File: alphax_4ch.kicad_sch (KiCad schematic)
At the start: 124 parts, among them J3 Conn_01x01, J4 Conn_01x01, J6 430451012, J7 Conn_01x01, J8 Conn_01x01, M1 Module-power_12and5V-0.1, M2 Module-ign8-0.2, M3 Module-vr-discrete-0.4, M6 Module-ign8-0.2, M8 Module-vr-discrete-0.4, M9 Module-knock-0.2, P1 33311-24AW-2, P2 33311-24AW-2, P3 Pad, P4 Pad

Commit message: Fab export
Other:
- note added: "4.5k UP (default)/3.3k DOWN"
- note added: "CAM HALL PU 5VA: remove R21 5VAS/GND configurable: - remove R4"
- note added: "Test note: IN_CRANK+ line HALL: remove R753_2 VR: remove R1126, R22"
- note added: "Test note: remove 1nf for VR"
- note removed: "1.2k UP (default)/4.5k DOWN"
- note removed: "CAM HALL PU 5VA: remove R21 5VAS configurable: - remove R4"
- note removed: "IN_CRANK+ line HALL: remove R753_2"
- note removed: "remove 1nf for VR"
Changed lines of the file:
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@@
   (title_block
     (title "AlphaECU 4chan powered by rusEFI")
-    (date "2023-03-19")
-    (rev "G")
+    (date "2023-05-11")
+    (rev "H")
     (company "rusEFI")
     (comment 7 "http://rusefi.com/s/alphax4ch")
@@
     (effects (font (size 1.27 1.27)) (justify left bottom))
   )
-  (text "1.2k UP (default)/4.5k DOWN" (at 299.72 255.27 0)
+  (text "4.5k UP (default)/3.3k DOWN" (at 299.72 255.27 0)
     (effects (font (size 1.27 1.27)) (justify left bottom))
   )
@@
     (effects (font (size 1.27 1.27)) (justify left bottom))
   )
-  (text "CAM HALL PU\n5VA: remove R21\n5VAS configurable: - remove R4"
+  (text "CAM HALL PU\n5VA: remove R21\n5VAS/GND configurable: - remove R4"
     (at 230.505 269.875 0)
     (effects (font (size 1.27 1.27)) (justify left bottom))
@@
     (effects (font (size 1.27 1.27)) (justify right bottom))
   )
+  (text "4.5k UP (default)/3.3k DOWN" (at 299.72 280.67 0)
+    (effects (font (size 1.27 1.27)) (justify left bottom))
+  )
   (text "GND test pads" (at 134.62 381 0)
     (effects (font (size 1.27 1.27)) (justify left bottom))
@@
     (effects (font (size 1.27 1.27)) (justify left bottom))
   )
-  (text "IN_CRANK+ line\nHALL: remove R753_2" (at 232.41 200.025 0)
-    (effects (font (size 1.27 1.27)) (justify left bottom))
-  )
-  (text "remove 1nf for VR" (at 241.3 179.705 0)
+  (text "Test note:\nIN_CRANK+ line\nHALL: remove R753_2\nVR: remove R1126, R22"
+    (at 229.87 200.66 0)
     (effects (font (size 1.27 1.27)) (justify left bottom))
   )
-  (text "1.2k UP (default)/4.5k DOWN" (at 299.72 280.67 0)
+  (text "Test note:\nremove 1nf for VR" (at 241.3 179.705 0)
     (effects (font (size 1.27 1.27)) (justify left bottom))
   )

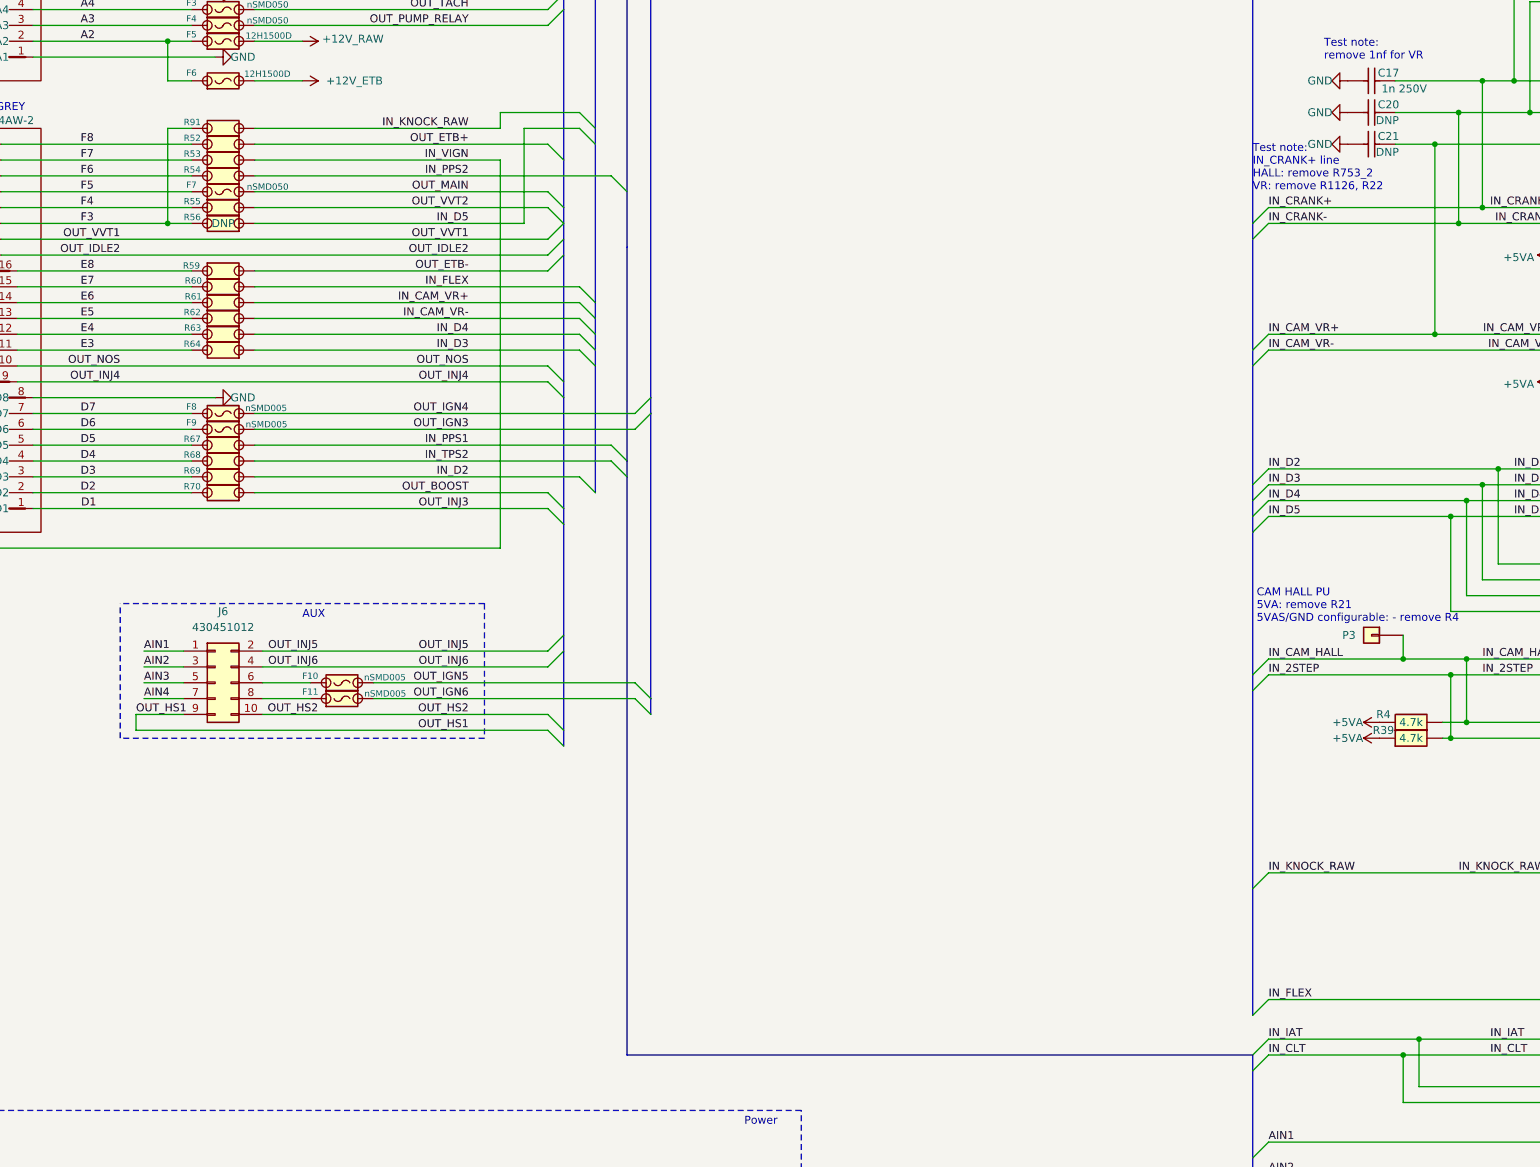
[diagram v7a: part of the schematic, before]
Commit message: VR caps, AUX conn symbol, HALL pullups resistors
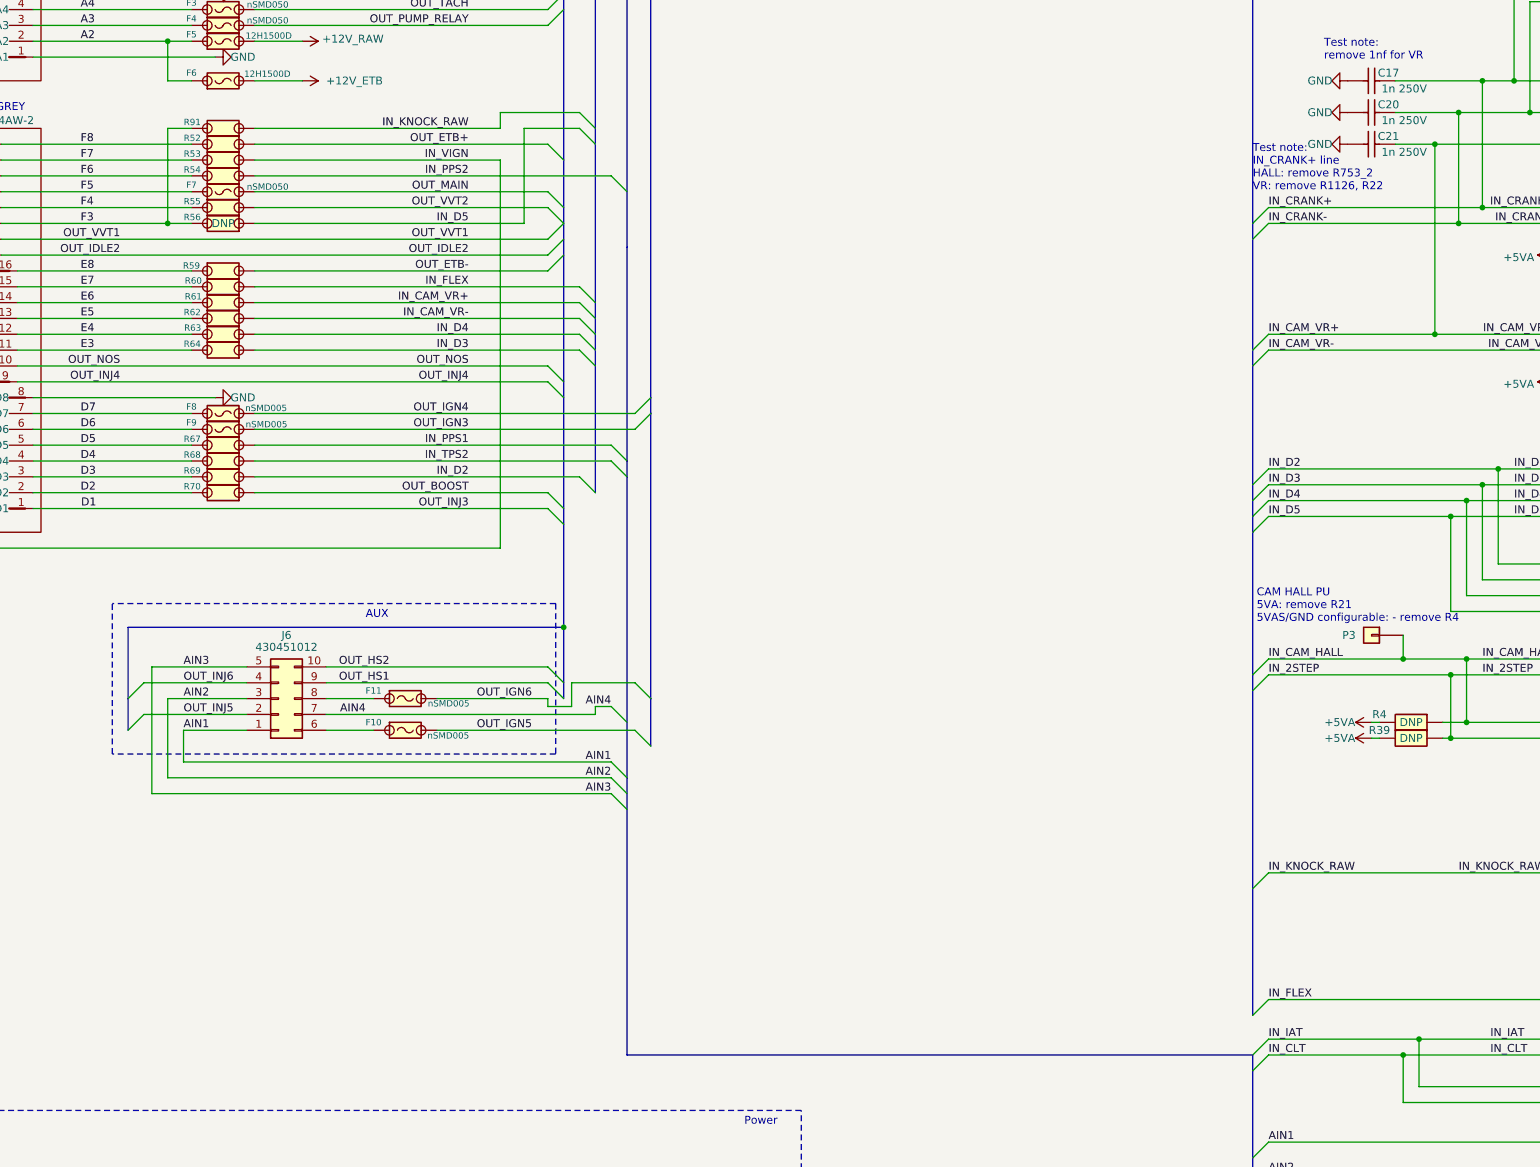
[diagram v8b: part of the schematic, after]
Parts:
- removed J6: 430451012, Connector_Molex:Molex_Micro-Fit_3.0_43045-1012_2x05_P3.00mm_Vertical, symbol Connector_Generic:Conn_02x05_Odd_Even
- added J6: 430451012, Connector_Molex:Molex_Micro-Fit_3.0_43045-1012_2x05_P3.00mm_Vertical, symbol Connector_Generic:Conn_02x05_Top_Bottom
- C20, C21: value ~ -> 1n 250V; LCSC (none) -> C277510; MyComment DNP -> (none)
- R39, R4: value 4.7k -> DNP; LCSC C23162 -> (none)
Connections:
- net +5VA: now also R39.2, R4.2; no longer R39.1, R4.1
- net AIN1: now also J6.1 (Pin_1)
- net AIN2: now also J6.3 (Pin_3)
- net AIN3: now also J6.5 (Pin_5)
- net AIN4: now also J6.7 (Pin_7)
- net IN_2STEP: now also R39.1; no longer R39.2
- net IN_CAM_HALL: now also R4.1; no longer R4.2
- net OUT_HS1: now also J6.9 (Pin_9)
- net OUT_HS2: now also J6.10 (Pin_10)
- net OUT_INJ5: now also J6.2 (Pin_2)
- net OUT_INJ6: now also J6.4 (Pin_4)
- net at F11.1: now also J6.8 (Pin_8)
- net at F10.1: now also J6.6 (Pin_6)
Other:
- moved on the sheet: F10, F11
